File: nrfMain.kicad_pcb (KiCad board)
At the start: 4 copper layers, 40 x 68.8 mm, 73 parts, among them J1 FTSH-105-01-F-DV-P-TR, J2 USB_C_Receptacle, J3 Conn_01x03, J4 Conn_01x04, J5 2337019-1, M1 Motor_Servo, M2 Motor_Servo, M3 Motor_Servo, M4 Motor_Servo, M5 Motor_Servo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

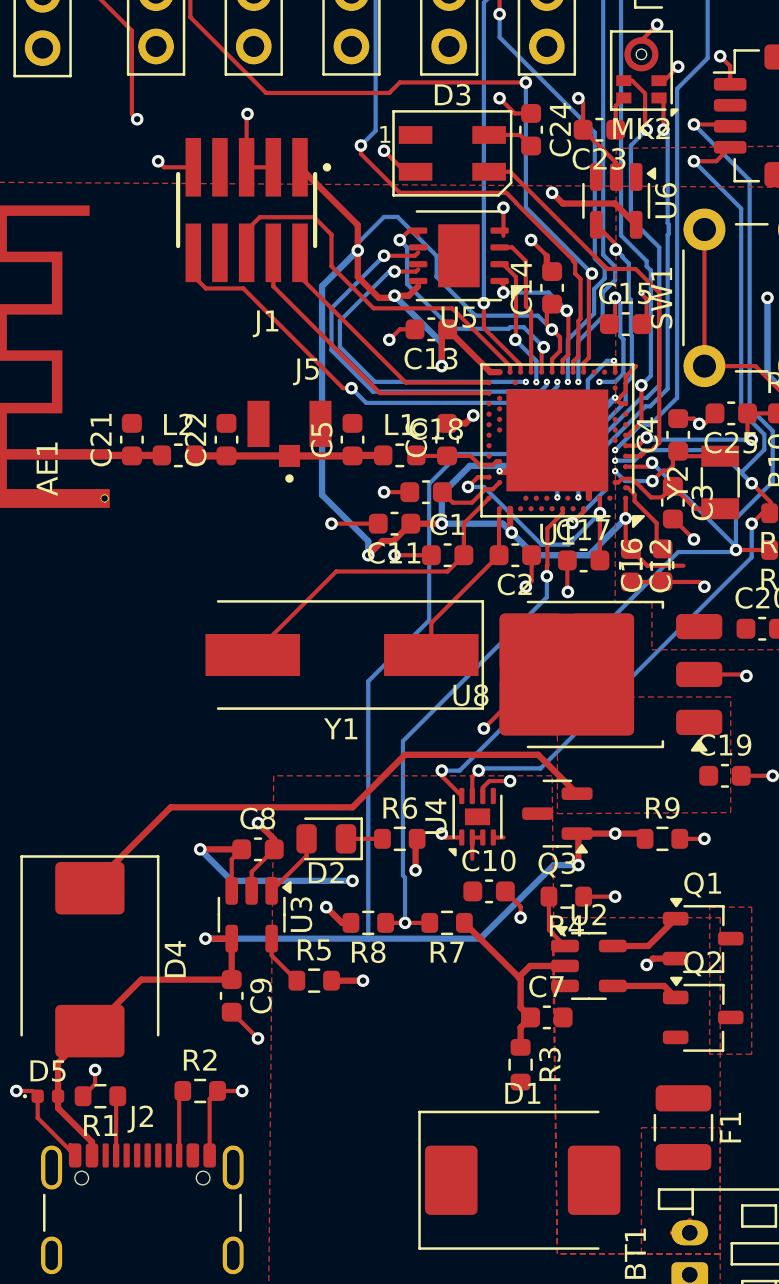
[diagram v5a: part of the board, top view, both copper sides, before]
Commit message: Added USB routing
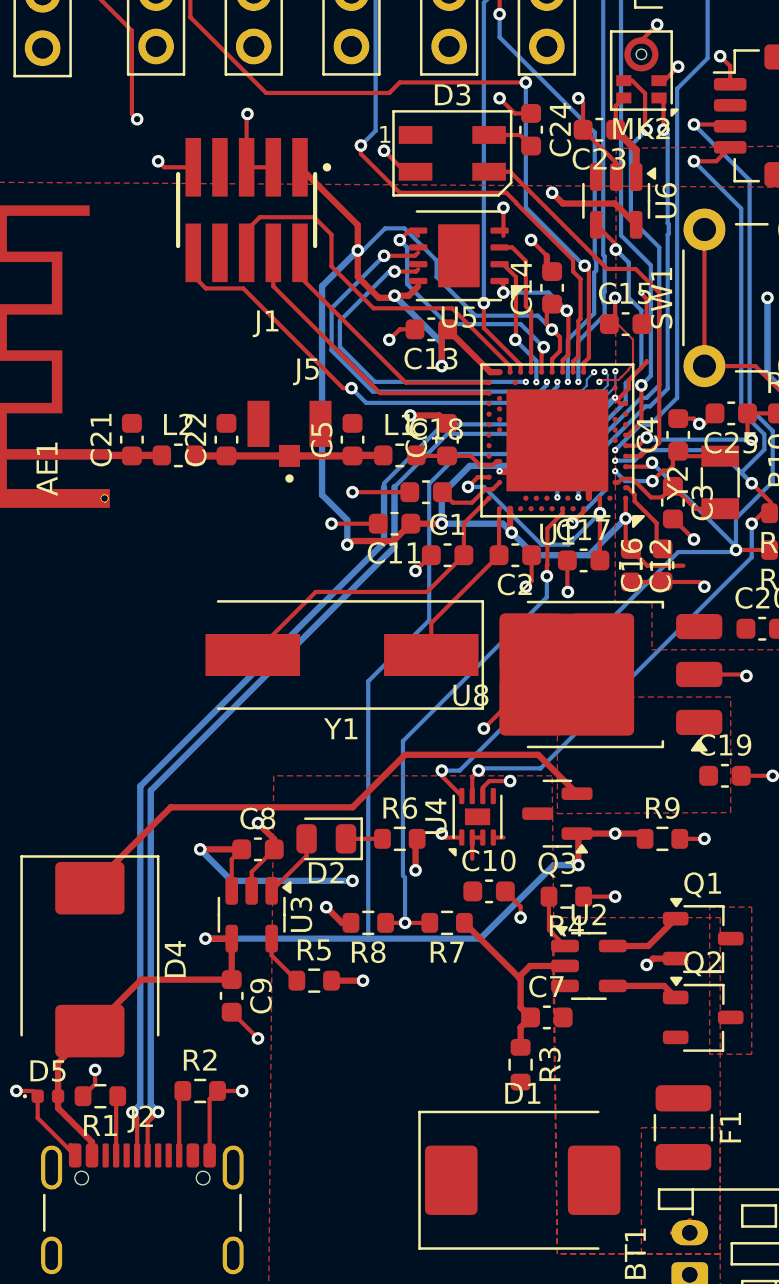
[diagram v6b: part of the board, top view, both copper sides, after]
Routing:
- net D_N: track 0.00 -> 49.8 mm, vias 0 -> 2
- net D_P: track 0.00 -> 49.4 mm, vias 0 -> 2
- net VDD: track 3.89 -> 6.55 mm
- net GND: track 85.4 -> 86.7 mm
- net VBUS: track 77.7 -> 76.6 mm

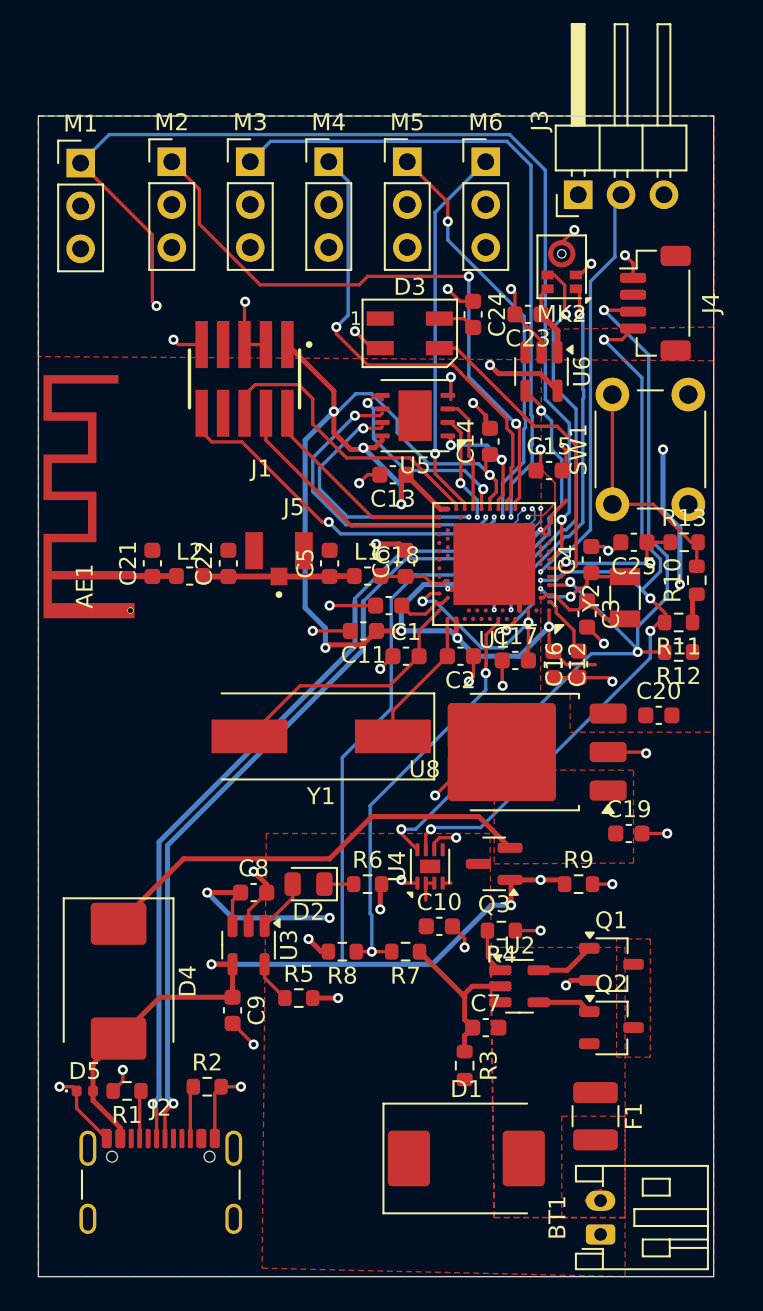
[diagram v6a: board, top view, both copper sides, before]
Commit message: Added mounting holes and other final touches
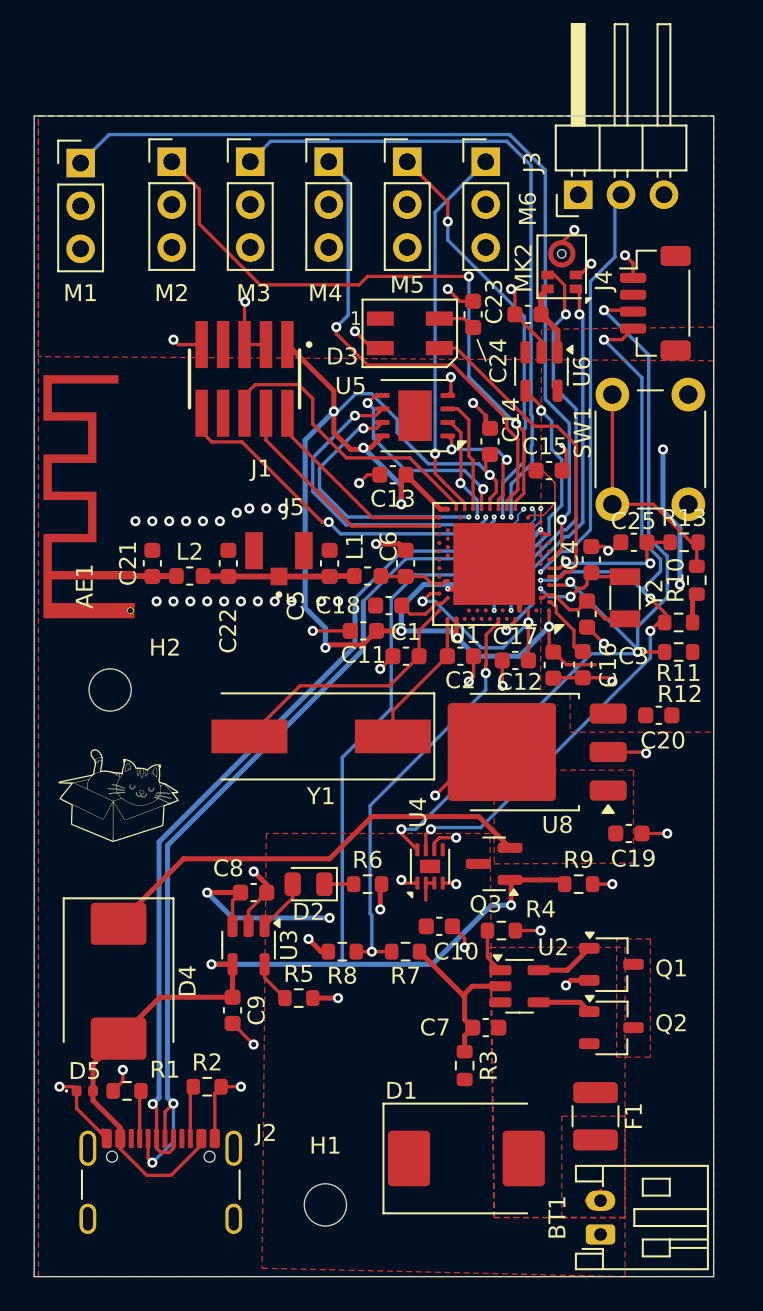
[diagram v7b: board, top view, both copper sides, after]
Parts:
- added G***: LOGO, Personal:cat, F.Cu at (62.5, 110.0)
- added H1: MountingHole, MountingHole:MountingHole_2.5mm, F.Cu at (74.8, 134.2)
- added H2: MountingHole, MountingHole:MountingHole_2.5mm, F.Cu at (62.0, 103.8)
- moved C16 0.25 mm to (90.0, 102.2)
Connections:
- J5 pad G2: (no net) -> GND
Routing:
- net PWM_0: track 63.6 -> 53.3 mm, vias 2 -> 1
- net VBUS: track 76.6 -> 83.8 mm, vias 4 -> 3
- net +3.3V: track 101.4 -> 94.3 mm, vias 12 -> 11
- net D_N: track 49.8 -> 55.4 mm, vias 2 -> 3
- net GND: track 86.7 -> 84.2 mm, vias 39 -> 60
- net D_P: track 49.4 -> 51.8 mm
- net Net-(U1-DECUSB): track 5.86 -> 4.66 mm, vias 2 -> 0
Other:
- board size 40 x 68.8 mm -> 40.2 x 68.8 mm
